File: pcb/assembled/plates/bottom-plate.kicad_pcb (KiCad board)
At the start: 2 copper layers, 114 x 97.8 mm, 16 parts, among them J1 MJ-4PP-9, J2 OLED

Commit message: Hotfix bottom plate
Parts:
- J1: footprint local:TRRS-PJ-320A-no-Fmask_cutout -> local:TRRS-PJ-320A_cutout
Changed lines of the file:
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@@
       (net 1 "GND"))
   )
-  (footprint "local:TRRS-PJ-320A-no-Fmask_cutout" (layer "F.Cu")
+  (footprint "local:TRRS-PJ-320A_cutout" (layer "F.Cu")
     (at 261.406021 121.704897 -90)
     (property "Sheetfile" "tako.kicad_sch")
@@
         (effects (font (size 1 1) (thickness 0.15)))
     )
-    (fp_line (start -3.05 0) (end -3.05 12.1)
-      (stroke (width 0.15) (type solid)) (layer "Dwgs.User"))
-    (fp_line (start -2.8 0) (end -2.8 -2)
-      (stroke (width 0.15) (type solid)) (layer "Dwgs.User"))
-    (fp_line (start 2.8 -2) (end -2.8 -2)
-      (stroke (width 0.15) (type solid)) (layer "Dwgs.User"))
-    (fp_line (start 2.8 0) (end 2.8 -2)
-      (stroke (width 0.15) (type solid)) (layer "Dwgs.User"))
-    (fp_line (start 3.05 0) (end -3.05 0)
-      (stroke (width 0.15) (type solid)) (layer "Dwgs.User"))
-    (fp_line (start 3.05 0) (end 3.05 12.1)
-      (stroke (width 0.15) (type solid)) (layer "Dwgs.User"))
-    (fp_line (start 3.05 12.1) (end -3.05 12.1)
-      (stroke (width 0.15) (type solid)) (layer "Dwgs.User"))
-    (fp_line (start -3.3 11.95) (end -3.3 10.65)
+    (fp_text user "Ring2" (at 0 3.25 -90) (layer "B.Fab")
+        (effects (font (size 0.7 0.7) (thickness 0.1)) (justify mirror))
+    )
+    (fp_text user "Sleeve" (at -0.25 11.4 -90) (layer "B.Fab")
+        (effects (font (size 0.7 0.7) (thickness 0.1)) (justify mirror))
+    )
+    (fp_text user "Tip" (at 0 10 -90) (layer "B.Fab")
+        (effects (font (size 0.7 0.7) (thickness 0.1)) (justify mirror))
+    )
+    (fp_text user "Ring1" (at 0 6.25 -90) (layer "B.Fab")
+        (effects (font (size 0.7 0.7) (thickness 0.1)) (justify mirror))
+    )
+    (fp_text user "Ring1" (at 0 6.25 -90) (layer "F.Fab")
+        (effects (font (size 0.7 0.7) (thickness 0.1)))
+    )
+    (fp_text user "Ring2" (at 0 3.25 -90) (layer "F.Fab")
+        (effects (font (size 0.7 0.7) (thickness 0.1)))
+    )
+    (fp_text user "Sleeve" (at 0.25 11.4 -90) (layer "F.Fab")
+        (effects (font (size 0.7 0.7) (thickness 0.1)))
+    )
+    (fp_text user "Tip" (at 0 10 -90) (layer "F.Fab")
+        (effects (font (size 0.7 0.7) (thickness 0.1)))
+    )
+    (fp_line (start -3.3 3.4) (end -3.3 3)
       (stroke (width 0.05) (type default)) (layer "Edge.Cuts"))
-    (fp_line (start -2.55 9.9) (end -2.05 9.9)
+    (fp_line (start -3.3 6.4) (end -3.3 6)
       (stroke (width 0.05) (type default)) (layer "Edge.Cuts"))
-    (fp_line (start -2.55 12.7) (end -2.05 12.7)
+    (fp_line (start -3.3 11.5) (end -3.3 10)
       (stroke (width 0.05) (type default)) (layer "Edge.Cuts"))
-    (fp_line (start -1.3 11.95) (end -1.3 10.65)
+    (fp_line (start -1.3 3) (end -1.3 3.4)
       (stroke (width 0.05) (type default)) (layer "Edge.Cuts"))
-    (fp_line (start 1.3 3.85) (end 1.3 2.55)
+    (fp_line (start -1.3 6) (end -1.3 6.4)
       (stroke (width 0.05) (type default)) (layer "Edge.Cuts"))
-    (fp_line (start 1.3 6.85) (end 1.3 5.55)
+    (fp_line (start -1.3 10) (end -1.3 11.5)
       (stroke (width 0.05) (type default)) (layer "Edge.Cuts"))
-    (fp_line (start 1.3 10.85) (end 1.3 9.55)
+    (fp_line (start 1.3 3) (end 1.3 3.4)
       (stroke (width 0.05) (type default)) (layer "Edge.Cuts"))
-    (fp_line (start 2.05 1.8) (end 2.55 1.8)
+    (fp_line (start 1.3 6) (end 1.3 6.4)
       (stroke (width 0.05) (type default)) (layer "Edge.Cuts"))
-    (fp_line (start 2.05 4.6) (end 2.55 4.6)
+    (fp_line (start 1.3 10) (end 1.3 11.6)
       (stroke (width 0.05) (type default)) (layer "Edge.Cuts"))
-    (fp_line (start 2.05 4.8) (end 2.55 4.8)
+    (fp_line (start 3.3 3.4) (end 3.3 3)
       (stroke (width 0.05) (type default)) (layer "Edge.Cuts"))
-    (fp_line (start 2.05 7.6) (end 2.55 7.6)
+    (fp_line (start 3.3 6.4) (end 3.3 6)
       (stroke (width 0.05) (type default)) (layer "Edge.Cuts"))
-    (fp_line (start 2.05 8.8) (end 2.55 8.8)
+    (fp_line (start 3.3 11.6) (end 3.3 10)
       (stroke (width 0.05) (type default)) (layer "Edge.Cuts"))
-    (fp_line (start 2.05 11.6) (end 2.55 11.6)
+    (fp_arc (start -3.3 3) (mid -2.3 2) (end -1.3 3)
       (stroke (width 0.05) (type default)) (layer "Edge.Cuts"))
-    (fp_line (start 3.3 3.85) (end 3.3 2.55)
+    (fp_arc (start -3.3 6) (mid -2.3 5) (end -1.3 6)
       (stroke (width 0.05) (type default)) (layer "Edge.Cuts"))
-    (fp_line (start 3.3 6.85) (end 3.3 5.55)
+    (fp_arc (start -3.3 10) (mid -2.3 9) (end -1.3 10)
       (stroke (width 0.05) (type default)) (layer "Edge.Cuts"))
-    (fp_line (start 3.3 10.85) (end 3.3 9.55)
+    (fp_arc (start -1.3 3.4) (mid -2.3 4.4) (end -3.3 3.4)
       (stroke (width 0.05) (type default)) (layer "Edge.Cuts"))
-    (fp_arc (start -3.3 10.65) (mid -3.08033 10.11967) (end -2.55 9.9)
+    (fp_arc (start -1.3 6.4) (mid -2.3 7.4) (end -3.3 6.4)
       (stroke (width 0.05) (type default)) (layer "Edge.Cuts"))
-    (fp_arc (start -2.55 12.7) (mid -3.08033 12.48033) (end -3.3 11.95)
+    (fp_arc (start -1.3 11.5) (mid -2.3 12.5) (end -3.3 11.5)
       (stroke (width 0.05) (type default)) (layer "Edge.Cuts"))
-    (fp_arc (start -2.05 9.9) (mid -1.51967 10.11967) (end -1.3 10.65)
+    (fp_arc (start 1.3 3) (mid 2.3 2) (end 3.3 3)
       (stroke (width 0.05) (type default)) (layer "Edge.Cuts"))
-    (fp_arc (start -1.3 11.95) (mid -1.51967 12.48033) (end -2.05 12.7)
+    (fp_arc (start 1.3 6) (mid 2.3 5) (end 3.3 6)
       (stroke (width 0.05) (type default)) (layer "Edge.Cuts"))
-    (fp_arc (start 1.3 2.55) (mid 1.51967 2.01967) (end 2.05 1.8)
+    (fp_arc (start 1.3 10) (mid 2.3 9) (end 3.3 10)
       (stroke (width 0.05) (type default)) (layer "Edge.Cuts"))
-    (fp_arc (start 1.3 5.55) (mid 1.51967 5.01967) (end 2.05 4.8)
+    (fp_arc (start 3.3 3.4) (mid 2.3 4.4) (end 1.3 3.4)
       (stroke (width 0.05) (type default)) (layer "Edge.Cuts"))
-    (fp_arc (start 1.3 9.55) (mid 1.51967 9.01967) (end 2.05 8.8)
+    (fp_arc (start 3.3 6.4) (mid 2.3 7.4) (end 1.3 6.4)
       (stroke (width 0.05) (type default)) (layer "Edge.Cuts"))
-    (fp_arc (start 2.05 4.6) (mid 1.51967 4.38033) (end 1.3 3.85)
+    (fp_arc (start 3.3 11.6) (mid 2.3 12.6) (end 1.3 11.6)
       (stroke (width 0.05) (type default)) (layer "Edge.Cuts"))
-    (fp_arc (start 2.05 7.6) (mid 1.51967 7.38033) (end 1.3 6.85)
-      (stroke (width 0.05) (type default)) (layer "Edge.Cuts"))
-    (fp_arc (start 2.05 11.6) (mid 1.51967 11.38033) (end 1.3 10.85)
-      (stroke (width 0.05) (type default)) (layer "Edge.Cuts"))
-    (fp_arc (start 2.55 1.8) (mid 3.08033 2.01967) (end 3.3 2.55)
-      (stroke (width 0.05) (type default)) (layer "Edge.Cuts"))
-    (fp_arc (start 2.55 4.8) (mid 3.08033 5.01967) (end 3.3 5.55)
-      (stroke (width 0.05) (type default)) (layer "Edge.Cuts"))
-    (fp_arc (start 2.55 8.8) (mid 3.08033 9.01967) (end 3.3 9.55)
-      (stroke (width 0.05) (type default)) (layer "Edge.Cuts"))
-    (fp_arc (start 3.3 3.85) (mid 3.08033 4.38033) (end 2.55 4.6)
-      (stroke (width 0.05) (type default)) (layer "Edge.Cuts"))
-    (fp_arc (start 3.3 6.85) (mid 3.08033 7.38033) (end 2.55 7.6)
-      (stroke (width 0.05) (type default)) (layer "Edge.Cuts"))
-    (fp_arc (start 3.3 10.85) (mid 3.08033 11.38033) (end 2.55 11.6)
-      (stroke (width 0.05) (type default)) (layer "Edge.Cuts"))
+    (model "../tako.3dshapes/PJ-320A.step"
+      (offset (xyz 0 0 0))
+      (scale (xyz 1 1 1))
+      (rotate (xyz -90 0 180))
+    )
   )
   (footprint "local:MountingHole_2.2mm_M2_Pad" (layer "F.Cu")

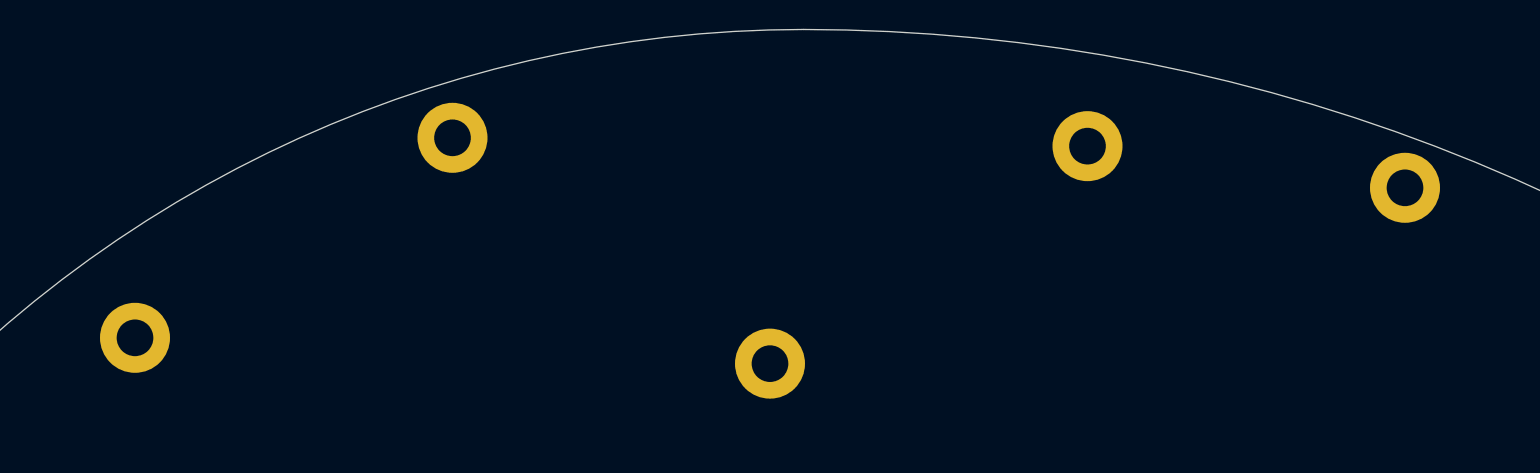
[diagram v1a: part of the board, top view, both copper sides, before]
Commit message: Align mounting holes to by in sync with diy version
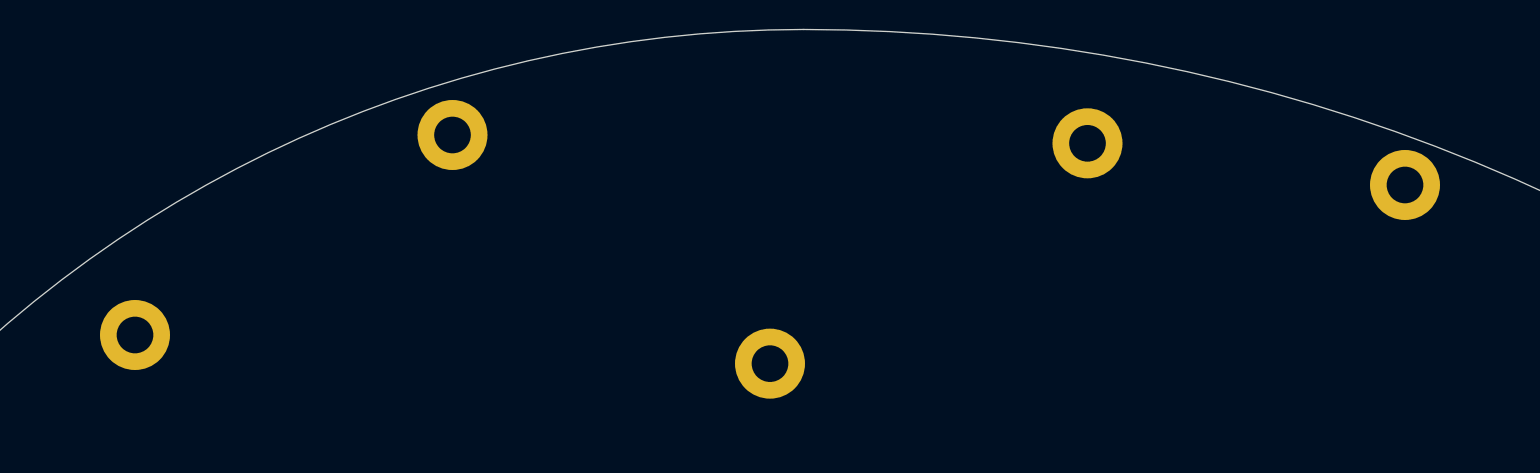
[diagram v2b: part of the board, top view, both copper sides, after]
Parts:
- moved H4 0.17 mm to (178.0, 56.6)
- moved H9 0.17 mm to (216.1, 57.1)
- moved H1 0.17 mm to (158.9, 68.6)
- moved H10 0.17 mm to (235.1, 59.6)
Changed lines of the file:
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@@
   )
   (footprint "local:MountingHole_2.2mm_M2_Pad" (layer "F.Cu")
-    (at 216.055485 57.237644)
+    (at 216.055485 57.0682)
     (descr "Mounting Hole 2.2mm, M2")
     (tags "mounting hole 2.2mm m2")
@@
   )
   (footprint "local:MountingHole_2.2mm_M2_Pad" (layer "F.Cu")
-    (at 235.105483 59.737639)
+    (at 235.105483 59.568195)
     (descr "Mounting Hole 2.2mm, M2")
     (tags "mounting hole 2.2mm m2")
@@
   )
   (footprint "local:MountingHole_2.2mm_M2_Pad" (layer "F.Cu")
-    (at 177.95548 56.738145)
+    (at 177.95548 56.568701)
     (descr "Mounting Hole 2.2mm, M2")
     (tags "mounting hole 2.2mm m2")
@@
   )
   (footprint "local:MountingHole_2.2mm_M2_Pad" (layer "F.Cu")
-    (at 158.905476 68.738141)
+    (at 158.905476 68.568697)
     (descr "Mounting Hole 2.2mm, M2")
     (tags "mounting hole 2.2mm m2")
